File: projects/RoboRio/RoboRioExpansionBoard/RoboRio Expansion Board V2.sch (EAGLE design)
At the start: 88 parts, among them CN1 PROP_PLUG, J1 RRINTERFACE-FEMALE, J2 MICROSD, Q1 5.0 MHz, T1 BC849, U1 P8X32A-Q44, U2 24LC256ST, U3 FT232RFTR232R, U4 MC1525TO

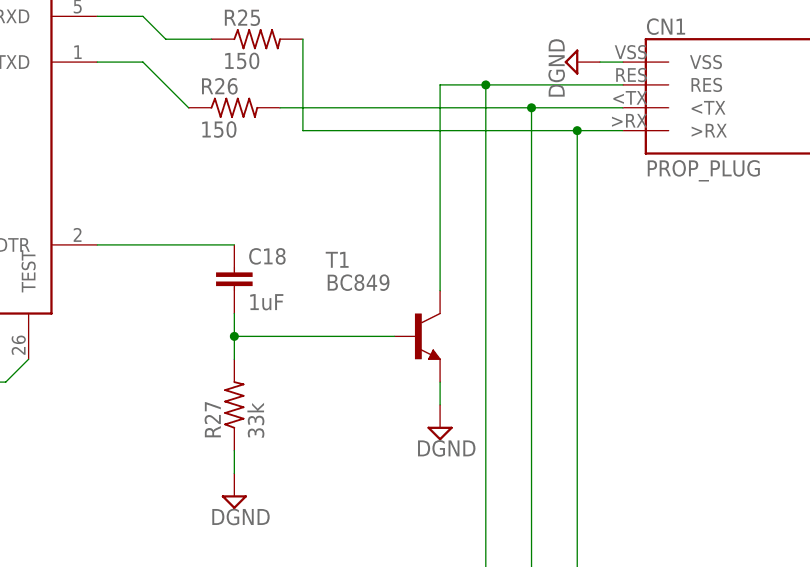
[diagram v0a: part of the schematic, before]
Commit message: Updated NPN transistor to new package
Note: SOT-416 = SC75
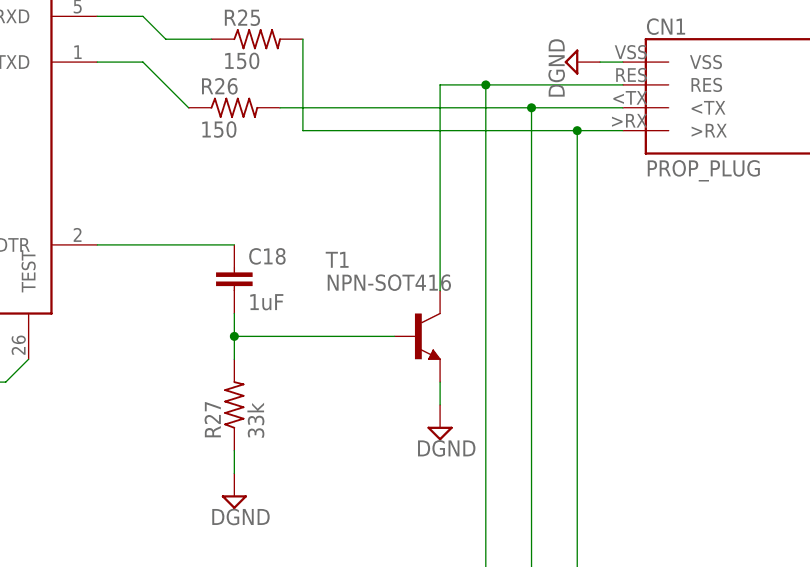
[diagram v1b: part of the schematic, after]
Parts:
- T1: value BC849 -> NPN-SOT416; device transistor:BC849 -> NPN transistor:NPN-SOT416
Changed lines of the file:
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@@
 <setting verticaltext="up"/>
 </settings>
-<grid distance="0.1" unitdist="inch" unit="inch" style="lines" multiple="1" display="no" altdistance="0.05" altunitdist="inch" altunit="inch"/>
+<grid distance="0.1" unitdist="inch" unit="inch" style="lines" multiple="1" display="no" altdistance="0.01" altunitdist="inch" altunit="inch"/>
 <layers>
-<layer number="1" name="Top" color="4" fill="1" visible="yes" active="no"/>
-<layer number="16" name="Bottom" color="1" fill="1" visible="yes" active="no"/>
-<layer number="17" name="Pads" color="2" fill="1" visible="yes" active="no"/>
-<layer number="18" name="Vias" color="2" fill="1" visible="yes" active="no"/>
-<layer number="19" name="Unrouted" color="6" fill="1" visible="yes" active="no"/>
-<layer number="20" name="Dimension" color="15" fill="1" visible="yes" active="no"/>
-<layer number="21" name="tPlace" color="7" fill="1" visible="yes" active="no"/>
-<layer number="22" name="bPlace" color="7" fill="1" visible="yes" active="no"/>
-<layer number="23" name="tOrigins" color="15" fill="1" visible="yes" active="no"/>
-<layer number="24" name="bOrigins" color="15" fill="1" visible="yes" active="no"/>
-<layer number="25" name="tNames" color="7" fill="1" visible="yes" active="no"/>
-<layer number="26" name="bNames" color="7" fill="1" visible="yes" active="no"/>
-<layer number="27" name="tValues" color="7" fill="1" visible="yes" active="no"/>
-<layer number="28" name="bValues" color="7" fill="1" visible="yes" active="no"/>
+<layer number="1" name="Top" color="4" fill="1" visible="no" active="no"/>
+<layer number="16" name="Bottom" color="1" fill="1" visible="no" active="no"/>
+<layer number="17" name="Pads" color="2" fill="1" visible="no" active="no"/>
+<layer number="18" name="Vias" color="2" fill="1" visible="no" active="no"/>
+<layer number="19" name="Unrouted" color="6" fill="1" visible="no" active="no"/>
+<layer number="20" name="Dimension" color="15" fill="1" visible="no" active="no"/>
+<layer number="21" name="tPlace" color="7" fill="1" visible="no" active="no"/>
+<layer number="22" name="bPlace" color="7" fill="1" visible="no" active="no"/>
+<layer number="23" name="tOrigins" color="15" fill="1" visible="no" active="no"/>
+<layer number="24" name="bOrigins" color="15" fill="1" visible="no" active="no"/>
+<layer number="25" name="tNames" color="7" fill="1" visible="no" active="no"/>
+<layer number="26" name="bNames" color="7" fill="1" visible="no" active="no"/>
+<layer number="27" name="tValues" color="7" fill="1" visible="no" active="no"/>
+<layer number="28" name="bValues" color="7" fill="1" visible="no" active="no"/>
 <layer number="29" name="tStop" color="7" fill="3" visible="no" active="no"/>
 <layer number="30" name="bStop" color="7" fill="6" visible="no" active="no"/>
@@
 <layer number="35" name="tGlue" color="7" fill="4" visible="no" active="no"/>
 <layer number="36" name="bGlue" color="7" fill="5" visible="no" active="no"/>
-<layer number="37" name="tTest" color="7" fill="1" visible="yes" active="no"/>
-<layer number="38" name="bTest" color="7" fill="1" visible="yes" active="no"/>
+<layer number="37" name="tTest" color="7" fill="1" visible="no" active="no"/>
+<layer number="38" name="bTest" color="7" fill="1" visible="no" active="no"/>
 <layer number="39" name="tKeepout" color="4" fill="11" visible="no" active="no"/>
 <layer number="40" name="bKeepout" color="1" fill="11" visible="no" active="no"/>
@@
 <layer number="44" name="Drills" color="7" fill="1" visible="no" active="no"/>
 <layer number="45" name="Holes" color="7" fill="1" visible="no" active="no"/>
-<layer number="46" name="Milling" color="3" fill="1" visible="yes" active="no"/>
-<layer number="47" name="Measures" color="7" fill="1" visible="yes" active="no"/>
-<layer number="48" name="Document" color="7" fill="1" visible="yes" active="no"/>
-<layer number="49" name="Reference" color="7" fill="1" visible="yes" active="no"/>
-<layer number="50" name="dxf" color="7" fill="1" visible="yes" active="no"/>
-<layer number="51" name="tDocu" color="7" fill="1" visible="yes" active="no"/>
-<layer number="52" name="bDocu" color="7" fill="1" visible="yes" active="no"/>
-<layer number="53" name="tGND_GNDA" color="7" fill="9" visible="yes" active="no"/>
-<layer number="54" name="bGND_GNDA" color="1" fill="9" visible="yes" active="no"/>
-<layer number="56" name="wert" color="7" fill="1" visible="yes" active="no"/>
-<layer number="57" name="tCAD" color="7" fill="1" visible="yes" active="no"/>
+<layer number="46" name="Milling" color="3" fill="1" visible="no" active="no"/>
+<layer number="47" name="Measures" color="7" fill="1" visible="no" active="no"/>
+<layer number="48" name="Document" color="7" fill="1" visible="no" active="no"/>
+<layer number="49" name="Reference" color="7" fill="1" visible="no" active="no"/>
+<layer number="50" name="dxf" color="7" fill="1" visible="no" active="no"/>
+<layer number="51" name="tDocu" color="7" fill="1" visible="no" active="no"/>
+<layer number="52" name="bDocu" color="7" fill="1" visible="no" active="no"/>
+<layer number="53" name="tGND_GNDA" color="7" fill="9" visible="no" active="no"/>
+<layer number="54" name="bGND_GNDA" color="1" fill="9" visible="no" active="no"/>
+<layer number="56" name="wert" color="7" fill="1" visible="no" active="no"/>
+<layer number="57" name="tCAD" color="7" fill="1" visible="no" active="no"/>
 <layer number="90" name="Modules" color="5" fill="1" visible="yes" active="yes"/>
 <layer number="91" name="Nets" color="2" fill="1" visible="yes" active="yes"/>
@@
 <part name="R27" library="resistor" deviceset="R-US_" device="R0603" value="33k"/>
 <part name="C18" library="resistor" deviceset="C-EU" device="C0603K" value="1uF"/>
-<part name="T1" library="transistor" deviceset="BC849" device=""/>
+<part name="T1" library="NPN transistor" deviceset="NPN-SOT416" device=""/>
 <part name="U1" library="parallax_propeller" deviceset="P8X32A-Q44" device=""/>
 <part name="SUPPLY15" library="supply2" deviceset="DGND" device=""/>

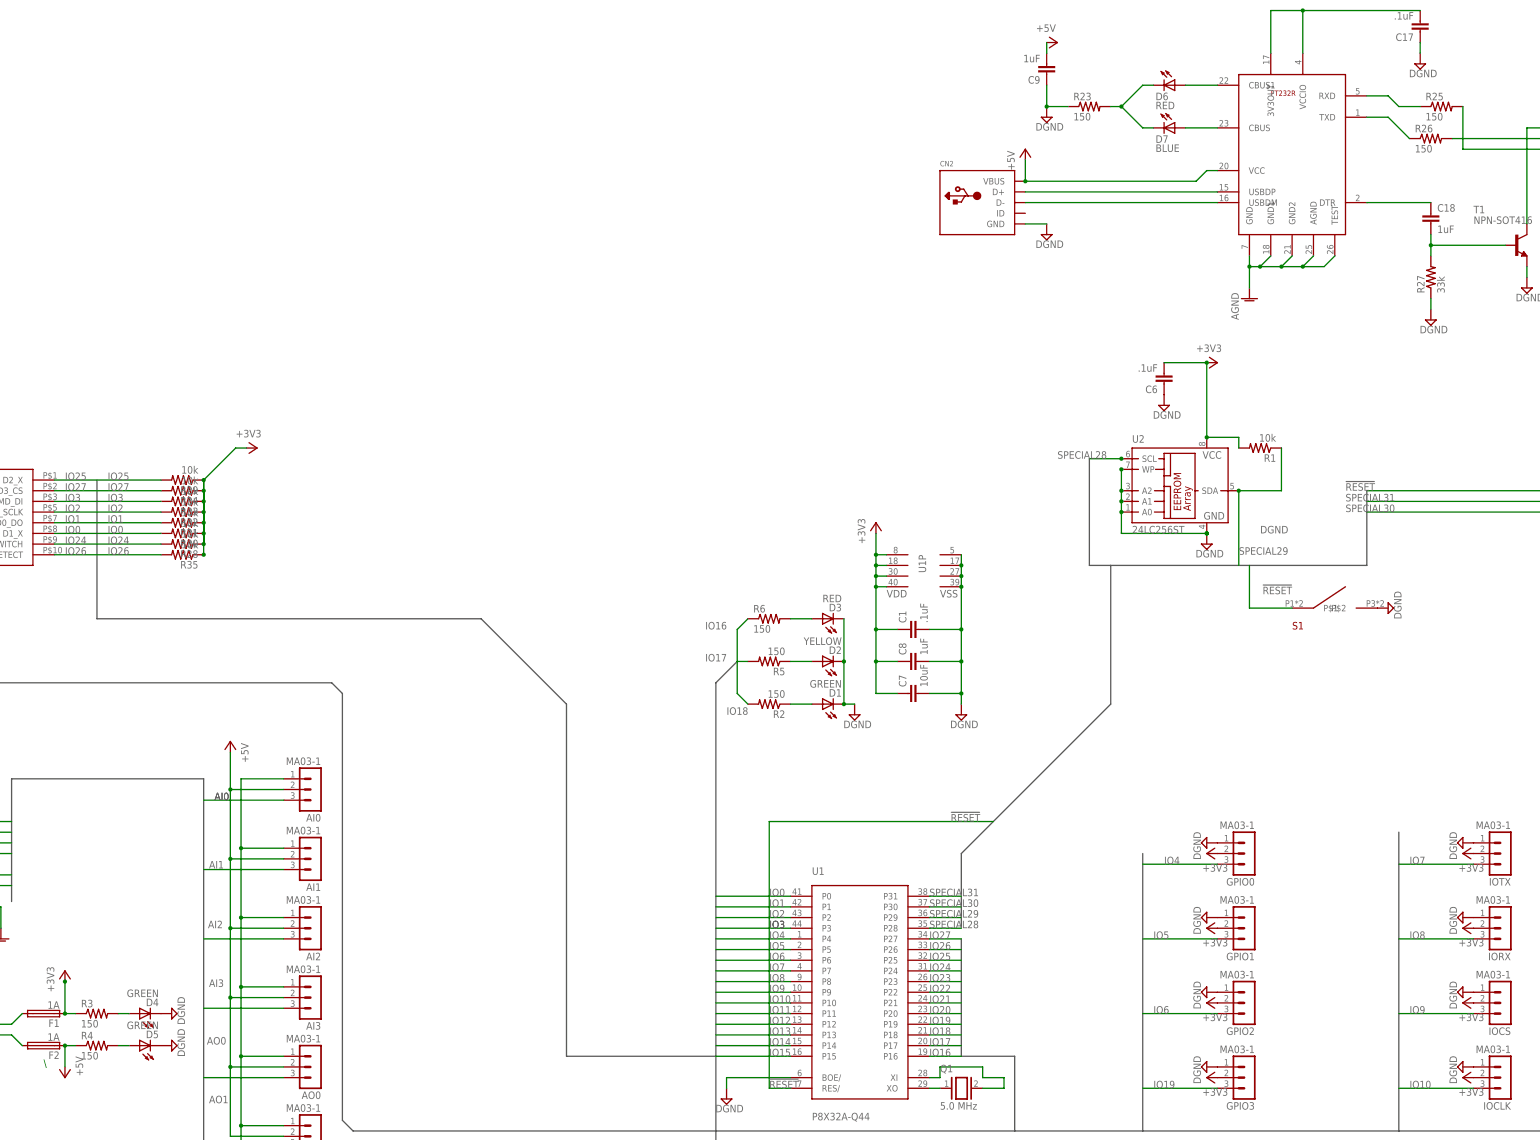
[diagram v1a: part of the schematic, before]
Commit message: Switched to a DIL resistor array
As required by available parts.
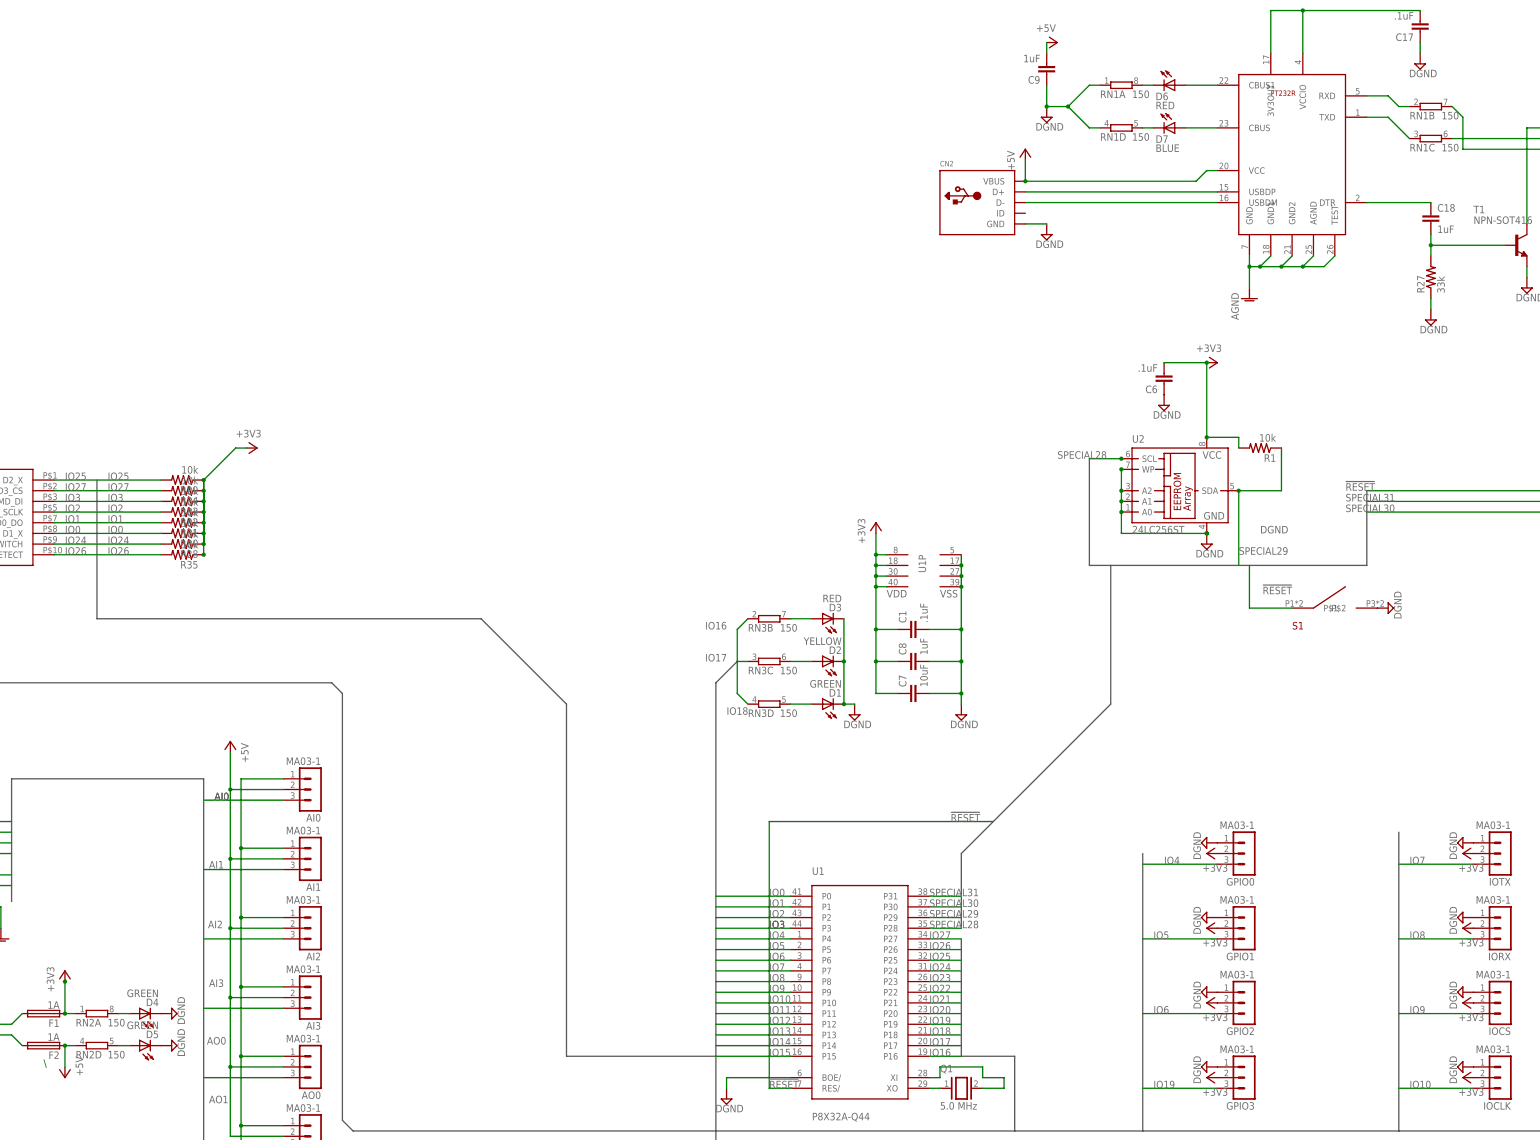
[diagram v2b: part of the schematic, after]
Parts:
- removed R2, R23, R25, R26, R3, R4, R5, R6: 150, resistor:R-US_R0603
- added RN1, RN2, RN3: 150, resistor-dil:4R-N0402ARV341
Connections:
- new net N$7: D6.C, RN1A.2
- net +3V3: now also RN2A.1; no longer R3.1
- net +5V: now also RN2D.1; no longer R4.1
- net DGND: now also RN1A.1, RN1D.1; no longer R23.1
- net IO16: now also RN3B.1; no longer R6.1
- net IO17: now also RN3C.1; no longer R5.2
- net IO18: now also RN3D.1; no longer R2.2
- net L1: now also RN2A.2; no longer R3.2
- net N$12: now also RN3B.2; no longer R6.2
- net N$13: now also RN3D.2; no longer R2.1
- net N$14: now also RN3C.2; no longer R5.1
- net N$18: now also RN1D.2; no longer D6.C, R23.2
- net N$23: now also RN1C.1; no longer R26.1
- net N$4: now also RN2D.2; no longer R4.2
- net N$6: now also RN1B.1; no longer R25.1
- net SPECIAL30: now also RN1B.2; no longer R25.2
- net SPECIAL31: now also RN1C.2; no longer R26.2
